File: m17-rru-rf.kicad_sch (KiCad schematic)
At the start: 0 parts

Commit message: Add files via upload
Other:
- sheet MCU ports: added nRST; removed none

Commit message: Add files via upload
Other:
- sheet MCU ports: added 3V3_IN, FWD_SENSE, PA_EN, REF_SENSE, RX_nCS, SPI_MISO, SPI_MOSI, SPI_SCK, TX_nCS; removed none
- sheet RF coupler ports: added FWD_RF, REF_RF; removed FWD_SENSE, REF_SENSE
- sheet RF detectors ports: added FWD_RF_IN, FWD_SENSE_OUT, REF_RF_IN, REF_SENSE_OUT; removed RF_FWD_DET, RF_FWD_IN, RF_REF_DET, RF_REF_IN

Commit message: Add files via upload
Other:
- sheet RF PA ports: added PA_EN_A, PA_EN_B; removed PA_EN

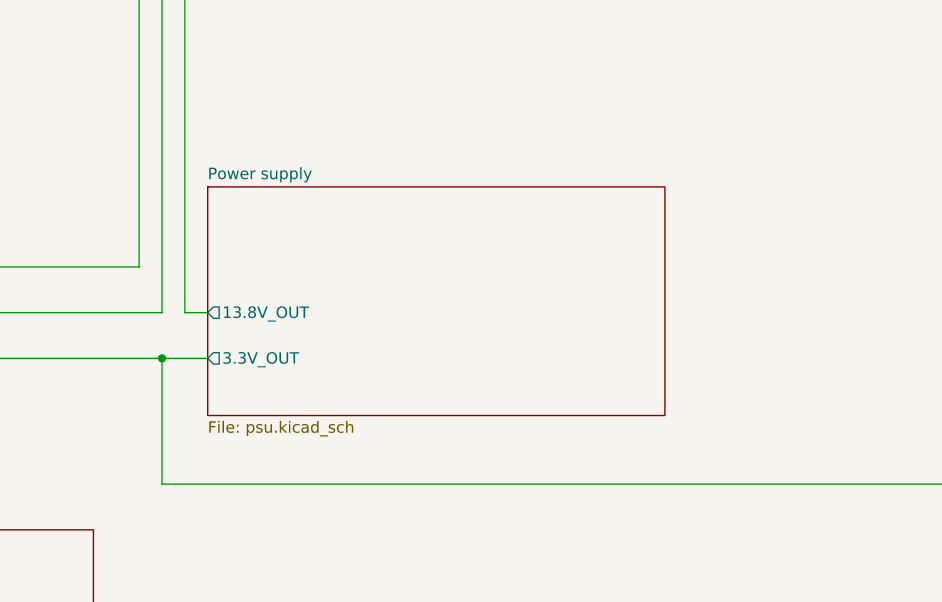
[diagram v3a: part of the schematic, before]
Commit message: LM317 protection diode location update
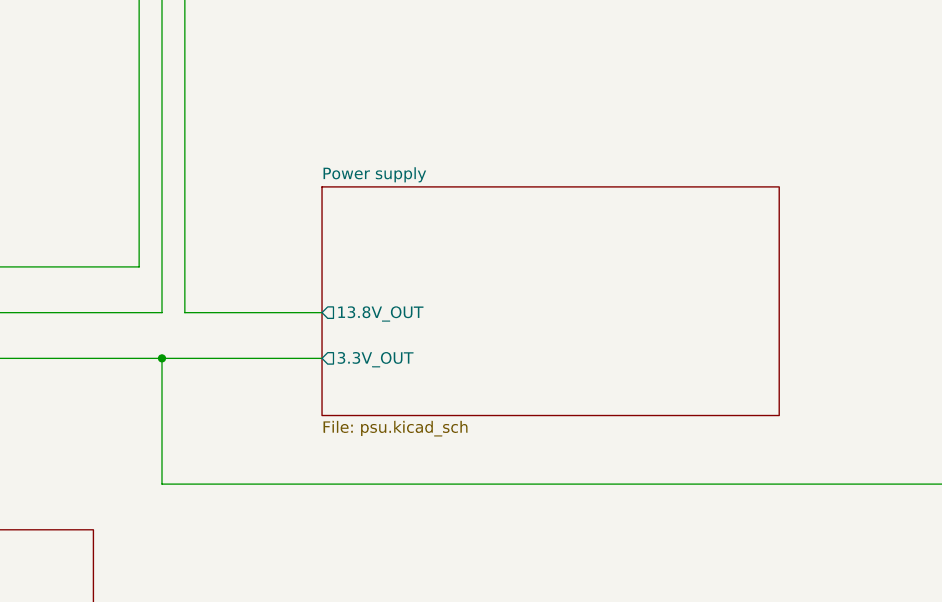
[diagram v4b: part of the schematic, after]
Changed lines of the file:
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@@
     (stroke (width 0) (type default))
   )
-  (wire (pts (xy 200.66 179.07) (xy 203.2 179.07))
+  (wire (pts (xy 200.66 179.07) (xy 215.9 179.07))
     (stroke (width 0) (type default))
   )
@@
     (stroke (width 0) (type default))
   )
-  (wire (pts (xy 198.12 184.15) (xy 203.2 184.15))
+  (wire (pts (xy 198.12 184.15) (xy 215.9 184.15))
     (stroke (width 0) (type default))
   )
@@
     )
   )
-  (sheet (at 203.2 165.1) (size 50.8 25.4) (fields_autoplaced)
-    (stroke (width 0.1524) (type solid))
-    (fill (color 0 0 0 0.0000))
-    (property "Sheetname" "Power supply" (at 203.2 164.3884 0)
-      (effects (font (size 1.27 1.27)) (justify left bottom))
-    )
-    (property "Sheetfile" "psu.kicad_sch" (at 203.2 191.0846 0)
-      (effects (font (size 1.27 1.27)) (justify left top))
-    )
-    (pin "13.8V_OUT" output (at 203.2 179.07 180)
-      (effects (font (size 1.27 1.27)) (justify left))
-    )
-    (pin "3.3V_OUT" output (at 203.2 184.15 180)
-      (effects (font (size 1.27 1.27)) (justify left))
-    )
+  (sheet (at 215.9 165.1) (size 50.8 25.4) (fields_autoplaced)
+    (stroke (width 0.1524) (type solid))
+    (fill (color 0 0 0 0.0000))
+    (property "Sheetname" "Power supply" (at 215.9 164.3884 0)
+      (effects (font (size 1.27 1.27)) (justify left bottom))
+    )
+    (property "Sheetfile" "psu.kicad_sch" (at 215.9 191.0846 0)
+      (effects (font (size 1.27 1.27)) (justify left top))
+    )
+    (pin "13.8V_OUT" output (at 215.9 179.07 180)
+      (effects (font (size 1.27 1.27)) (justify left))
+    )
+    (pin "3.3V_OUT" output (at 215.9 184.15 180)
+      (effects (font (size 1.27 1.27)) (justify left))
+    )

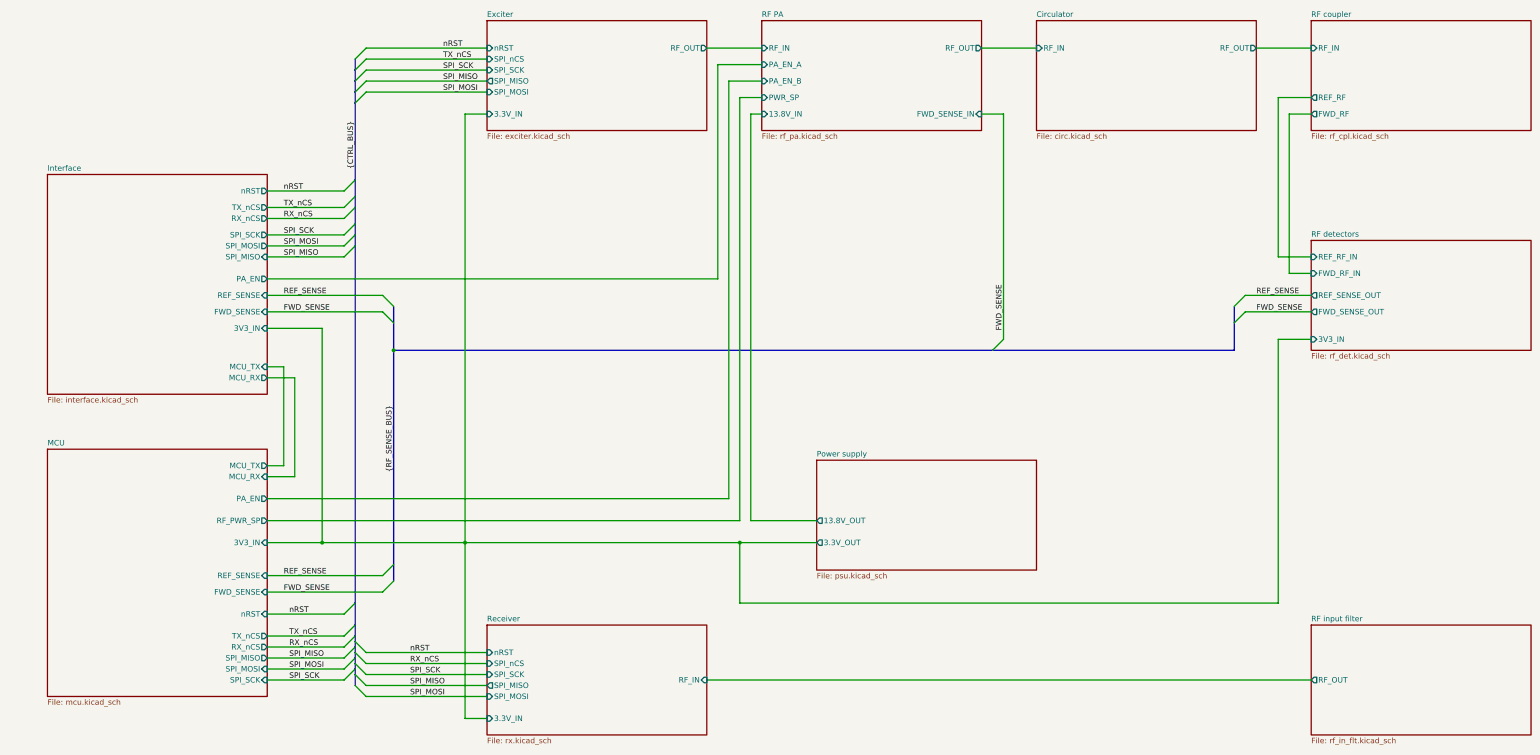
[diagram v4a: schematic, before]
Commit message: added missing 40MHz source
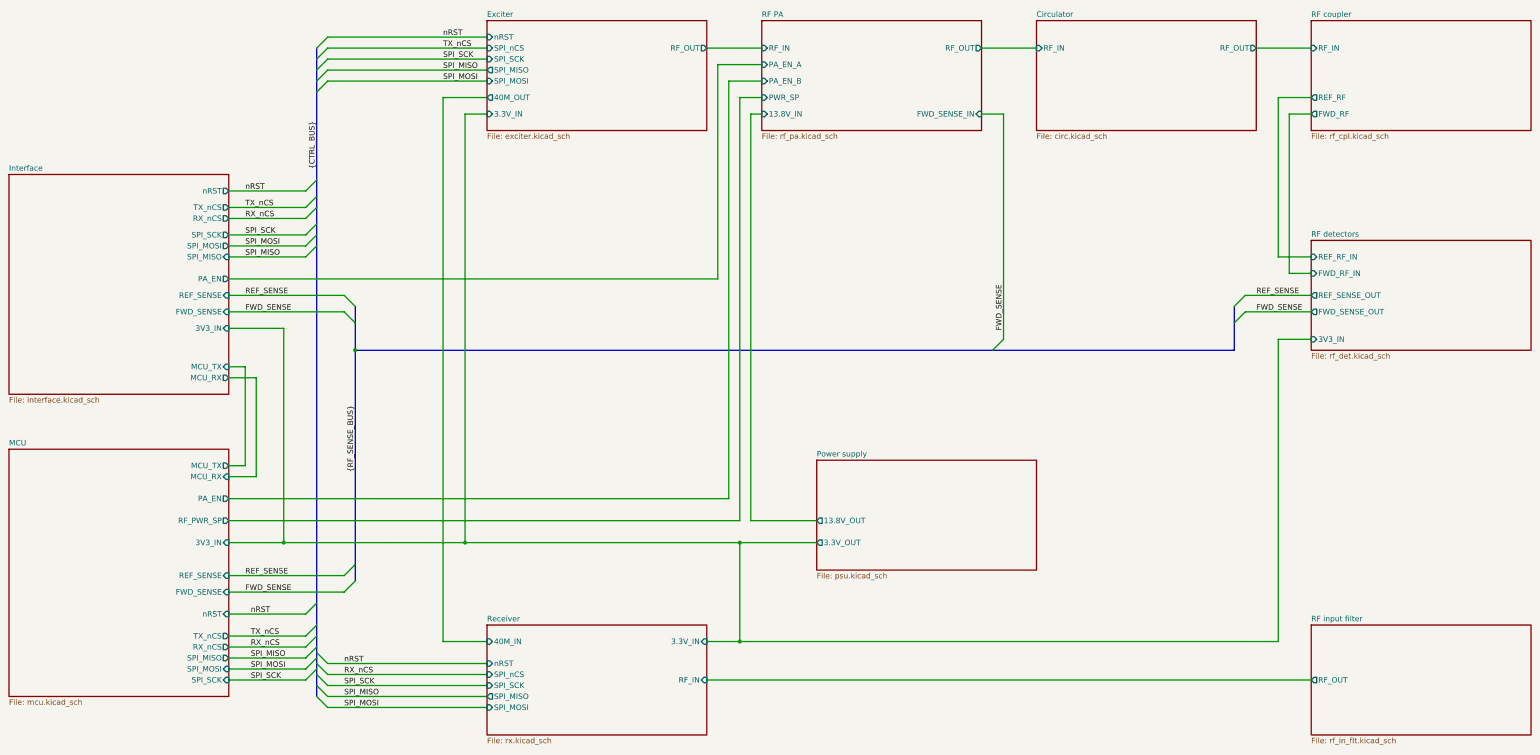
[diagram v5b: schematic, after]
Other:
- sheet Exciter ports: added 40M_OUT; removed none
- sheet Receiver ports: added 40M_IN; removed none

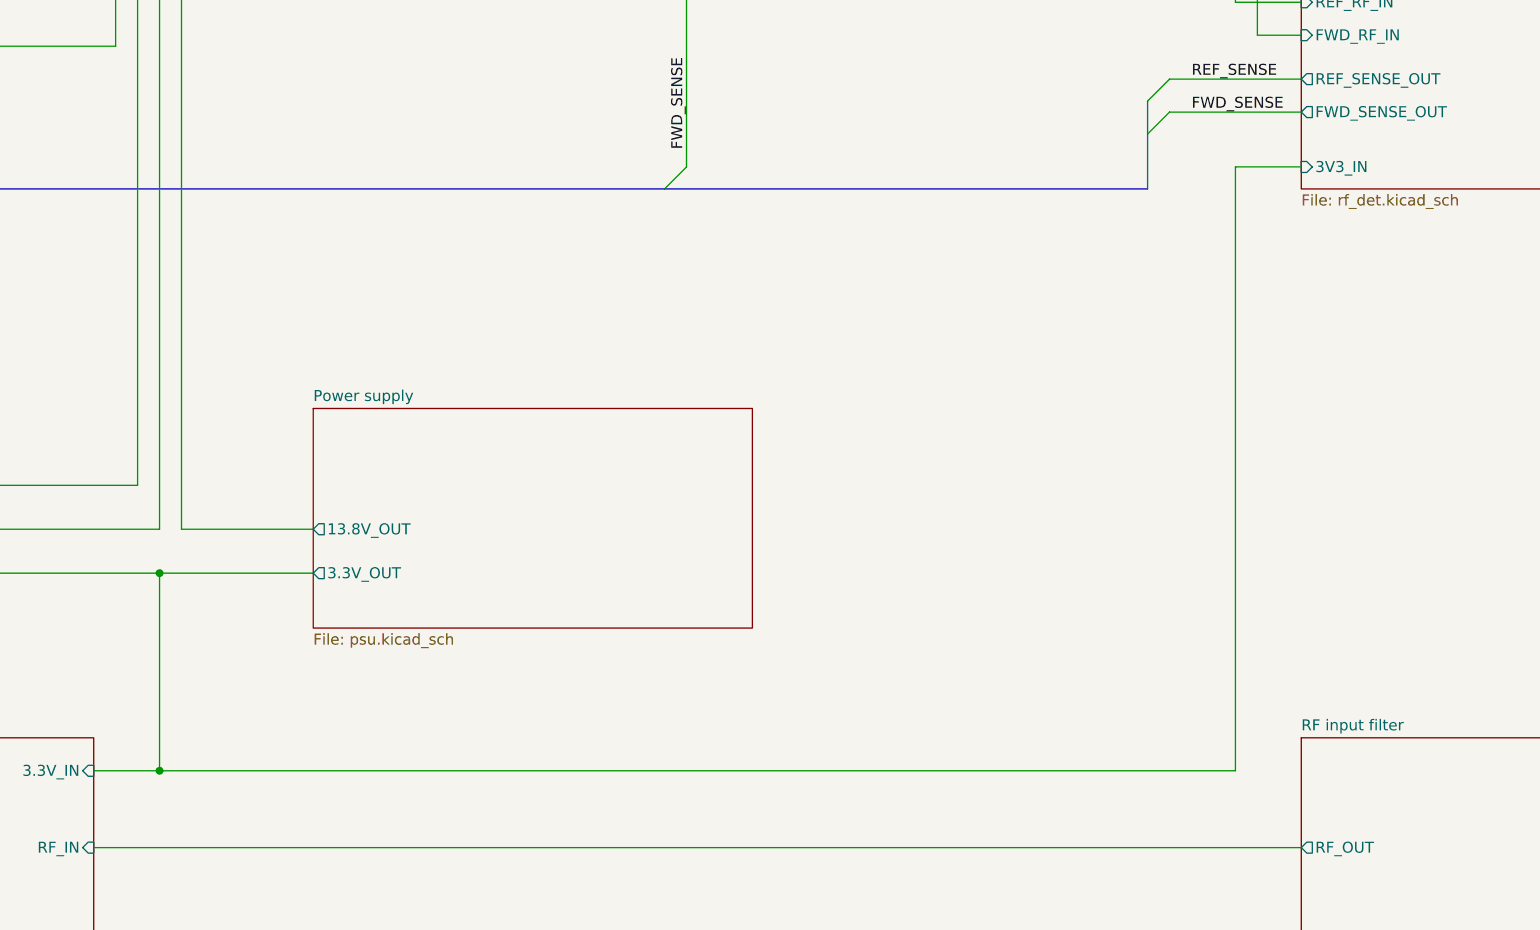
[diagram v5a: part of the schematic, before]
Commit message: significant updates
- supply for the detector block changed from 3.3V to 5V
- minor bugfixes
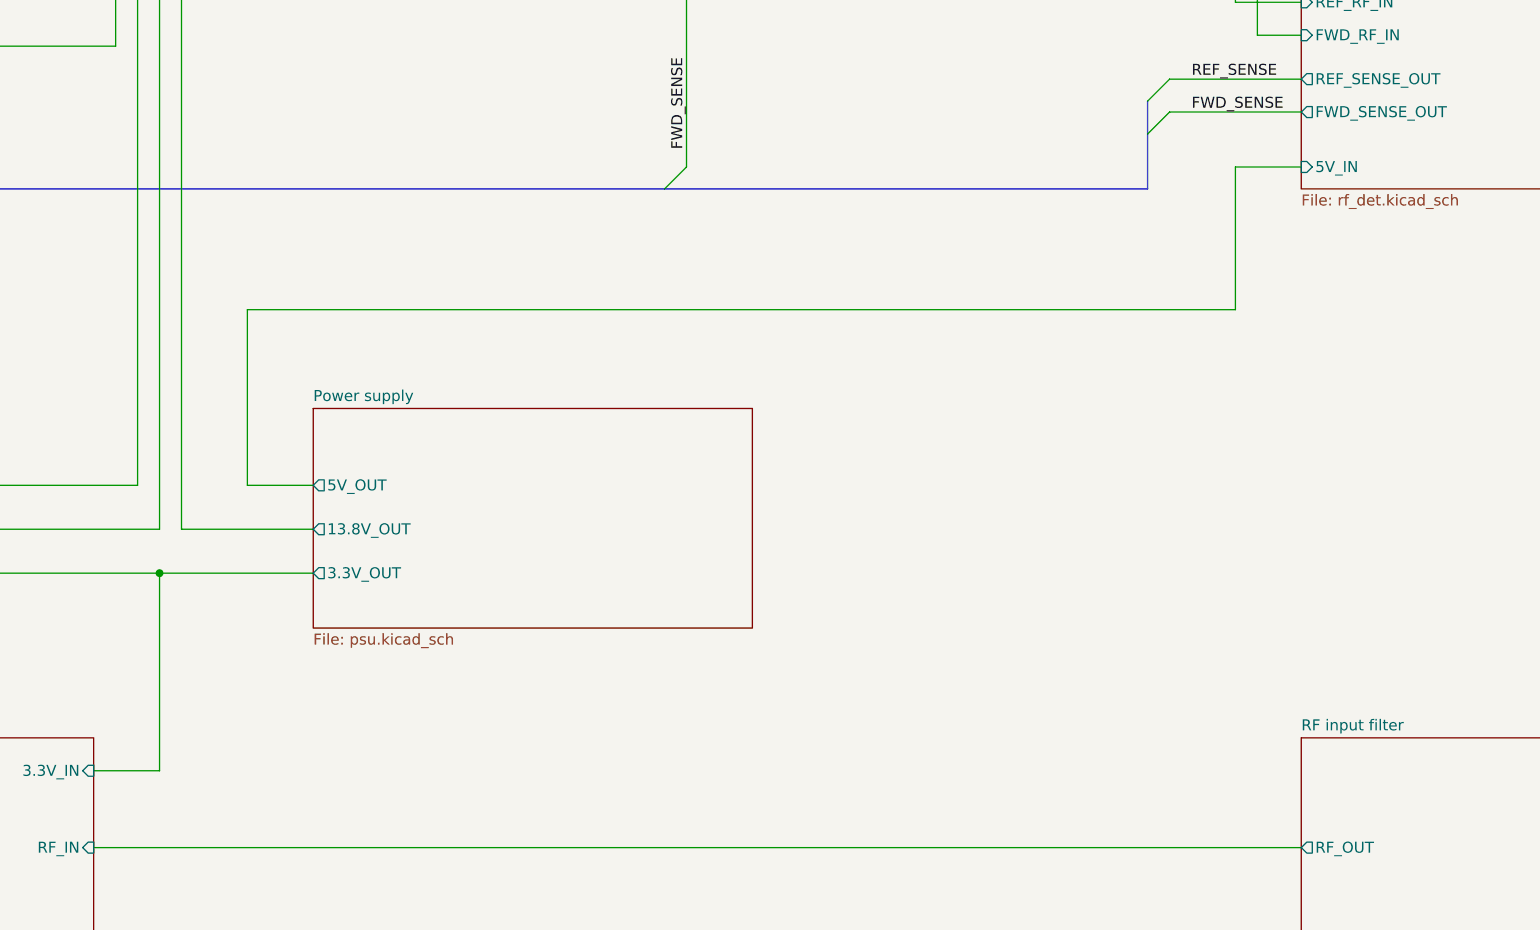
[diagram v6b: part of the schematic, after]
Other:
- sheet Power supply ports: added 5V_OUT; removed none
- sheet RF detectors ports: added 5V_IN; removed 3V3_IN
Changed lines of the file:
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@@
   (junction (at 198.12 184.15) (diameter 0) (color 0 0 0 0)
   )
-  (junction (at 198.12 207.01) (diameter 0) (color 0 0 0 0)
-  )
   (bus_entry (at 109.22 193.04) (size -2.54 2.54)
     (stroke (width 0) (type default))
@@
     (stroke (width 0) (type default))
   )
-  (wire (pts (xy 322.58 207.01) (xy 198.12 207.01))
-    (stroke (width 0) (type default))
-  )
   (wire (pts (xy 134.62 85.09) (xy 139.7 85.09))
     (stroke (width 0) (type default))
@@
     (stroke (width 0) (type default))
   )
+  (wire (pts (xy 208.28 153.67) (xy 322.58 153.67))
+    (stroke (width 0) (type default))
+  )
+  (wire (pts (xy 208.28 173.99) (xy 208.28 153.67))
+    (stroke (width 0) (type default))
+  )
   (wire (pts (xy 195.58 77.47) (xy 195.58 173.99))
     (stroke (width 0) (type default))
@@
     (stroke (width 0) (type default))
   )
+  (wire (pts (xy 322.58 153.67) (xy 322.58 137.16))
+    (stroke (width 0) (type default))
+  )
   (wire (pts (xy 102.87 72.39) (xy 139.7 72.39))
     (stroke (width 0) (type default))
@@
     (stroke (width 0) (type default))
   )
-  (wire (pts (xy 322.58 137.16) (xy 322.58 207.01))
-    (stroke (width 0) (type default))
-  )
   (wire (pts (xy 200.66 85.09) (xy 203.2 85.09))
     (stroke (width 0) (type default))
@@
   )
   (wire (pts (xy 330.2 81.28) (xy 322.58 81.28))
+    (stroke (width 0) (type default))
+  )
+  (wire (pts (xy 215.9 173.99) (xy 208.28 173.99))
     (stroke (width 0) (type default))
   )
@@
       (effects (font (size 1.27 1.27)) (justify left))
     )
+    (pin "5V_OUT" output (at 215.9 173.99 180)
+      (effects (font (size 1.27 1.27)) (justify left))
+    )
     (instances
       (project "m17-rru-rf"
@@
       (effects (font (size 1.27 1.27)) (justify left))
     )
-    (pin "3V3_IN" input (at 330.2 137.16 180)
-      (effects (font (size 1.27 1.27)) (justify left))
-    )
+    (pin "5V_IN" input (at 330.2 137.16 180)
+      (effects (font (size 1.27 1.27)) (justify left))
+    )

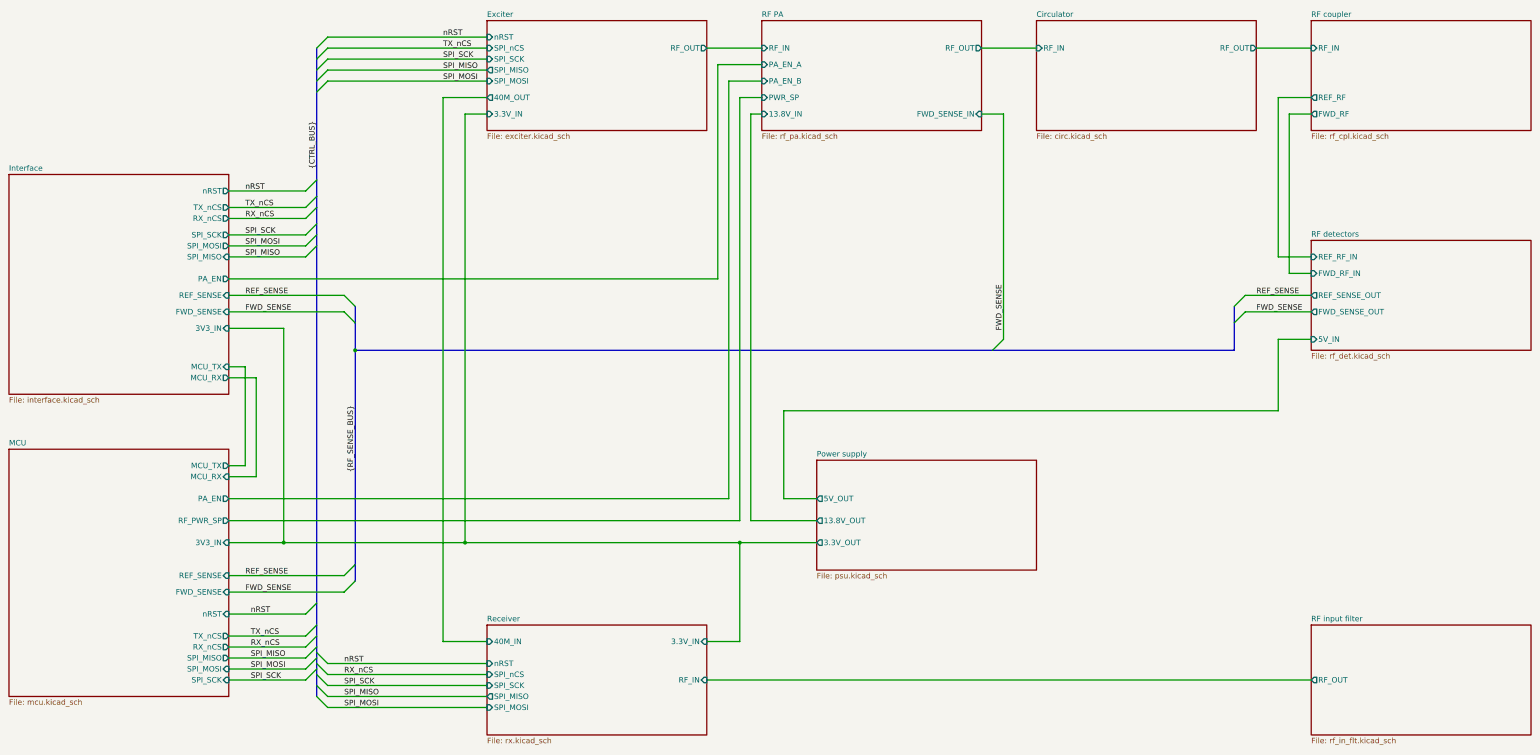
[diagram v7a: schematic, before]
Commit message: TP updates, temp sensor added
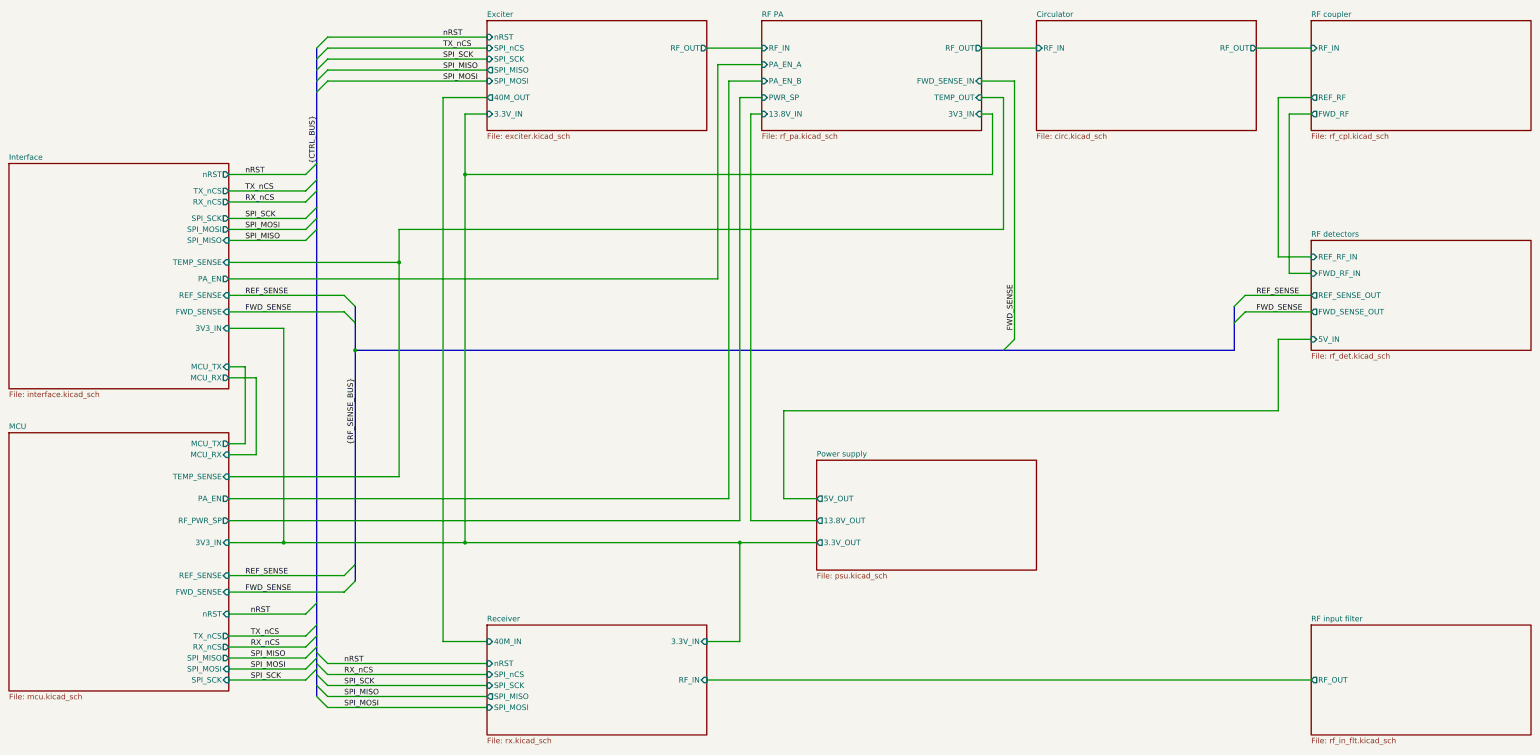
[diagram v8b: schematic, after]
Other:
- sheet Interface ports: added TEMP_SENSE; removed none
- sheet MCU ports: added TEMP_SENSE; removed none
- sheet RF PA ports: added 3V3_IN, TEMP_OUT; removed none
